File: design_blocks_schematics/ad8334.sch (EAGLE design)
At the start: 68 parts, among them IC1 AD8334ACPZ

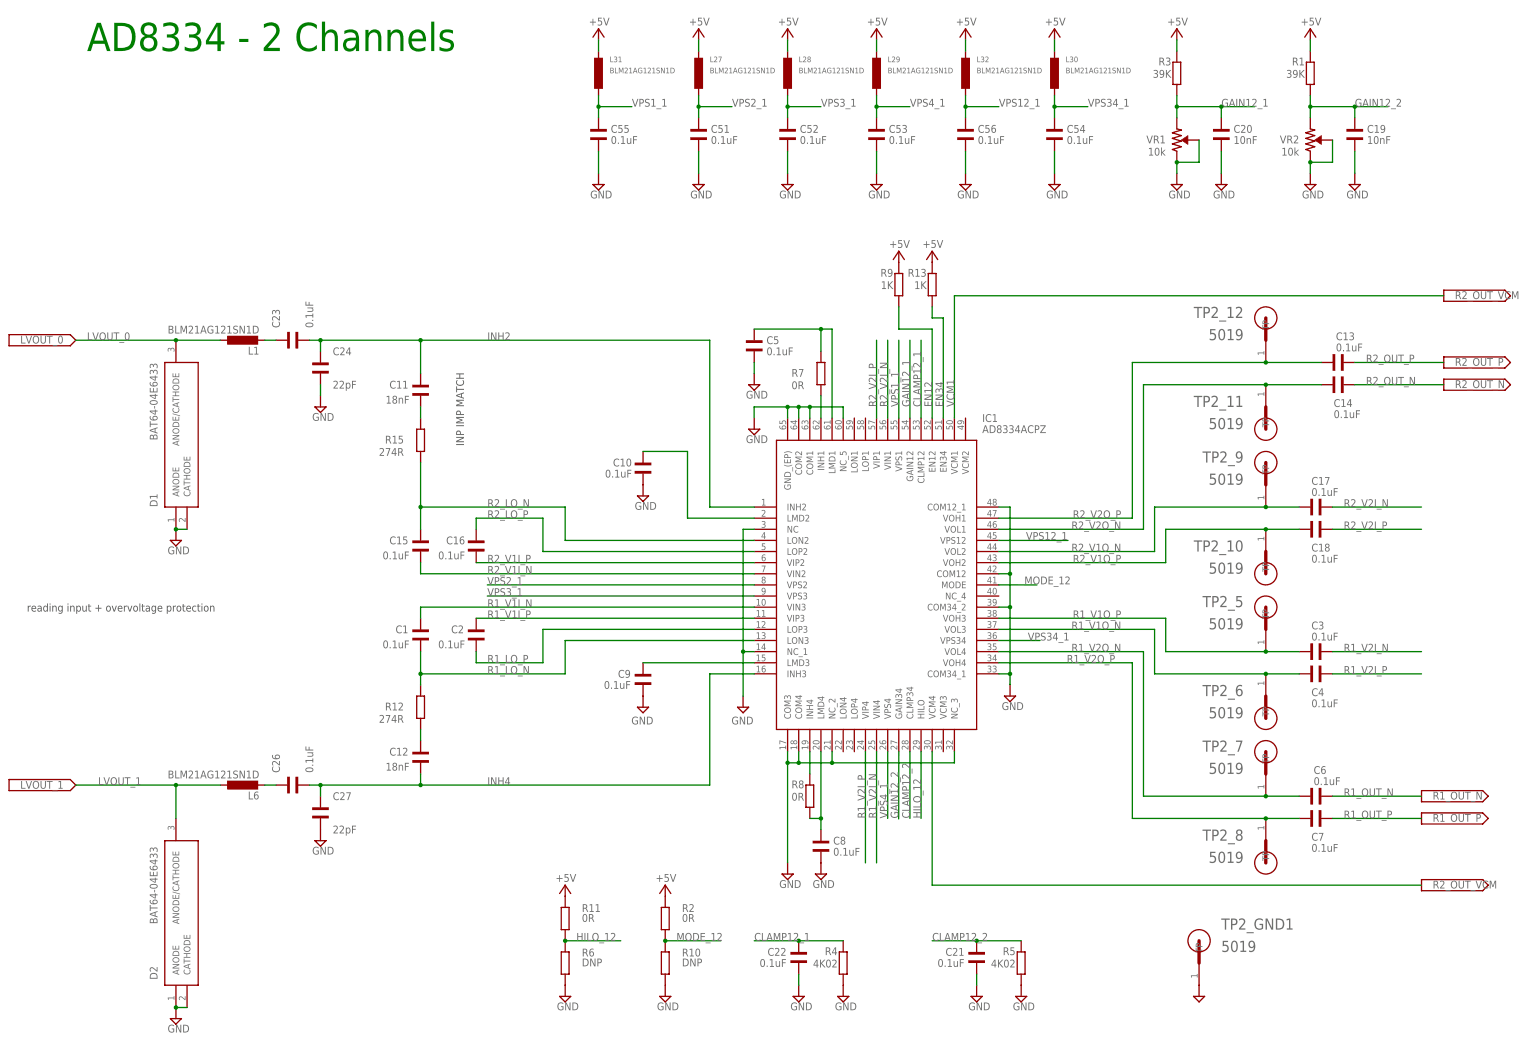
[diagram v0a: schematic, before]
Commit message: updated input/output net names
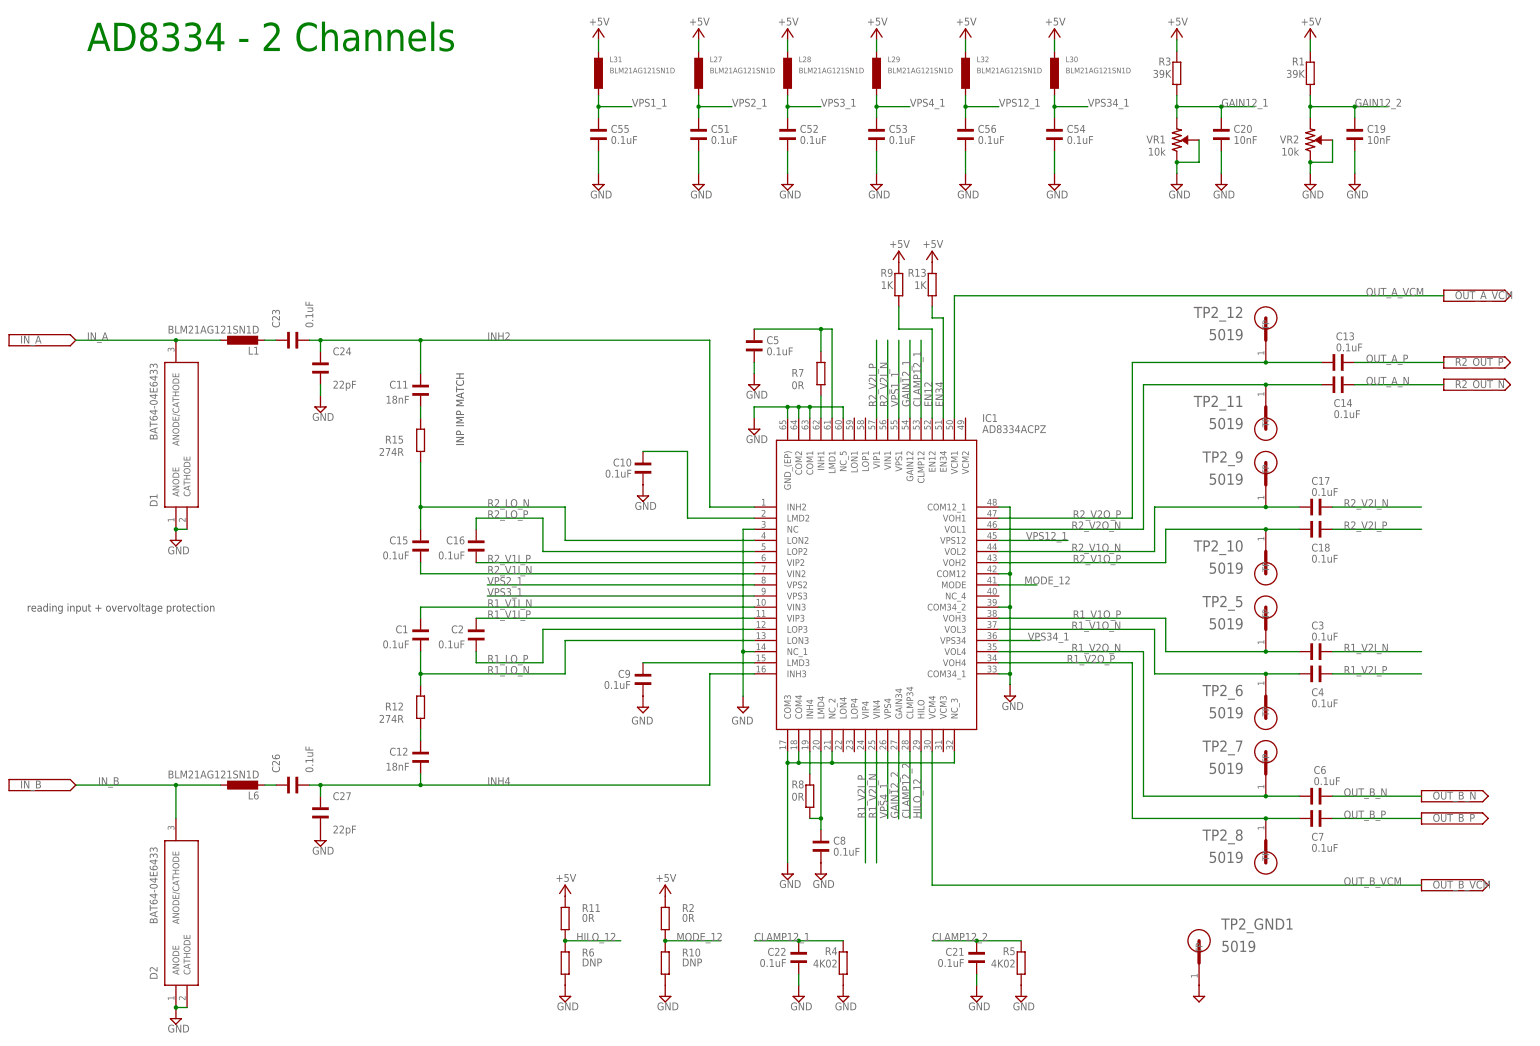
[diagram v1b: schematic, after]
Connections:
- net LVOUT_0 renamed IN_A
- net LVOUT_1 renamed IN_B
- net R1_OUT_N renamed OUT_B_N
- net R1_OUT_P renamed OUT_B_P
- net R2_OUT_N renamed OUT_A_N
- net R2_OUT_P renamed OUT_A_P
- net VCM1 renamed OUT_A_VCM
- net VCM3 renamed OUT_B_VCM
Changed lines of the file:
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@@
 <setting verticaltext="up"/>
 </settings>
-<grid distance="1" unitdist="mm" unit="mm" style="lines" multiple="1" display="no" altdistance="0.5" altunitdist="mm" altunit="mm"/>
+<grid distance="0.1" unitdist="inch" unit="inch" style="lines" multiple="1" display="yes" altdistance="0.01" altunitdist="inch" altunit="inch"/>
 <layers>
 <layer number="1" name="Top" color="4" fill="1" visible="no" active="no"/>
@@
 <part name="FRAME1" library="frames" library_urn="urn:adsk.eagle:library:229" deviceset="A3L-LOC" device=""/>
 <part name="SUPPLY5" library="supply2" library_urn="urn:adsk.eagle:library:372" deviceset="V--&gt;" device="">
-<attribute name="NET" value="LVOUT_0"/>
+<attribute name="NET" value="IN_A"/>
 </part>
 <part name="SUPPLY6" library="supply2" library_urn="urn:adsk.eagle:library:372" deviceset="GND" device=""/>
@@
 <part name="C2" library="Wurth_Elektronik_Passive_Capacitors_rev18b" library_urn="urn:adsk.eagle:library:491551" deviceset="WCAP-CSGP_0402" device="" package3d_urn="urn:adsk.eagle:package:491821/2" technology="_885012205037" value="0.1uF"/>
 <part name="SUPPLY8" library="supply2" library_urn="urn:adsk.eagle:library:372" deviceset="V--&gt;" device="">
-<attribute name="NET" value="LVOUT_0"/>
+<attribute name="NET" value="IN_B"/>
 </part>
 <part name="SUPPLY3" library="supply2" library_urn="urn:adsk.eagle:library:372" deviceset="GND" device=""/>
@@
 </part>
 <part name="SUPPLY17" library="supply2" library_urn="urn:adsk.eagle:library:372" deviceset="V--&gt;" device="">
-<attribute name="NET" value="R1_OUT_N"/>
+<attribute name="NET" value="OUT_B_N"/>
 </part>
 <part name="SUPPLY18" library="supply2" library_urn="urn:adsk.eagle:library:372" deviceset="V--&gt;" device="">
-<attribute name="NET" value="R1_OUT_P"/>
+<attribute name="NET" value="OUT_B_P"/>
 </part>
 <part name="SUPPLY25" library="supply2" library_urn="urn:adsk.eagle:library:372" deviceset="GND" device=""/>
 <part name="SUPPLY9" library="supply2" library_urn="urn:adsk.eagle:library:372" deviceset="V--&gt;" device="">
-<attribute name="NET" value="R2_OUT_VCM"/>
+<attribute name="NET" value="OUT_A_VCM"/>
 </part>
 <part name="SUPPLY10" library="supply2" library_urn="urn:adsk.eagle:library:372" deviceset="V--&gt;" device="">
-<attribute name="NET" value="R2_OUT_VCM"/>
+<attribute name="NET" value="OUT_B_VCM"/>
 </part>
 <part name="P+1" library="supply1" library_urn="urn:adsk.eagle:library:371" deviceset="+5V" device=""/>
@@
 <instance part="SUPPLY8" gate="G$1" x="5.08" y="68.58" smashed="yes">
 <attribute name="VALUE" x="6.35" y="67.818" size="1.778" layer="96" display="off"/>
+<attribute name="NET" x="7.62" y="67.818" size="1.778" layer="96"/>
 </instance>
 <instance part="SUPPLY3" gate="GND" x="43.18" y="124.46" smashed="yes">
@@
 </segment>
 </net>
-<net name="VCM1" class="0">
+<net name="OUT_A_VCM" class="0">
 <segment>
 <pinref part="IC1" gate="G$1" pin="VCM1"/>
 <wire x1="220.98" y1="152.4" x2="220.98" y2="180.34" width="0.1524" layer="91"/>
-<label x="220.98" y="154.94" size="1.778" layer="95" rot="R270" align="top-right"/>
+<label x="314.96" y="180.34" size="1.778" layer="95" rot="R180" align="top-right"/>
 <wire x1="220.98" y1="180.34" x2="332.74" y2="180.34" width="0.1524" layer="91"/>
 </segment>
@@
 </segment>
 </net>
-<net name="LVOUT_1" class="2">
-<segment>
-<label x="25.4" y="68.58" size="1.778" layer="95" rot="R180" align="top-right"/>
-<pinref part="D2" gate="G$1" pin="ANODE/CATHODE"/>
-<pinref part="L6" gate="G$1" pin="1"/>
-<wire x1="53.34" y1="68.58" x2="43.18" y2="68.58" width="0.1524" layer="91"/>
-<wire x1="43.18" y1="68.58" x2="20.32" y2="68.58" width="0.1524" layer="91"/>
-<wire x1="43.18" y1="60.96" x2="43.18" y2="68.58" width="0.1524" layer="91"/>
-<junction x="43.18" y="68.58"/>
-</segment>
-<segment>
-<label x="7.62" y="67.7418" size="1.778" layer="95" rot="R180" align="top-right"/>
-</segment>
-</net>
 <net name="VPS1_1" class="0">
 <segment>
@@
 </segment>
 </net>
-<net name="LVOUT_0" class="0">
+<net name="IN_A" class="0">
 <segment>
 <pinref part="D1" gate="G$1" pin="ANODE/CATHODE"/>
@@
 </segment>
 </net>
-<net name="R1_OUT_N" class="0">
+<net name="OUT_B_N" class="0">
 <segment>
 <pinref part="C6" gate="G$1" pin="2"/>
@@
 </segment>
 </net>
-<net name="R1_OUT_P" class="0">
+<net name="OUT_B_P" class="0">
 <segment>
 <pinref part="C7" gate="G$1" pin="2"/>
@@
 </segment>
 </net>
-<net name="R2_OUT_P" class="0">
+<net name="OUT_A_P" class="0">
 <segment>
 <pinref part="C13" gate="G$1" pin="2"/>
@@
 </segment>
 </net>
-<net name="R2_OUT_N" class="0">
+<net name="OUT_A_N" class="0">
 <segment>
 <pinref part="C14" gate="G$1" pin="2"/>
@@
 </segment>
 </net>
-<net name="VCM3" class="0">
+<net name="OUT_B_VCM" class="0">
 <segment>
 <wire x1="215.9" y1="45.72" x2="327.66" y2="45.72" width="0.1524" layer="91"/>
 <pinref part="IC1" gate="G$1" pin="VCM4"/>
 <wire x1="215.9" y1="76.2" x2="215.9" y2="45.72" width="0.1524" layer="91"/>
+<label x="309.88" y="45.72" size="1.778" layer="95"/>
 </segment>
 </net>
@@
 </segment>
 </net>
+<net name="IN_B" class="2">
+<segment>
+<label x="25.4" y="68.58" size="1.778" layer="95" rot="R180" align="top-right"/>
+<pinref part="D2" gate="G$1" pin="ANODE/CATHODE"/>
+<pinref part="L6" gate="G$1" pin="1"/>
+<wire x1="53.34" y1="68.58" x2="43.18" y2="68.58" width="0.1524" layer="91"/>
+<wire x1="43.18" y1="68.58" x2="20.32" y2="68.58" width="0.1524" layer="91"/>
+<wire x1="43.18" y1="60.96" x2="43.18" y2="68.58" width="0.1524" layer="91"/>
+<junction x="43.18" y="68.58"/>
+</segment>
+</net>

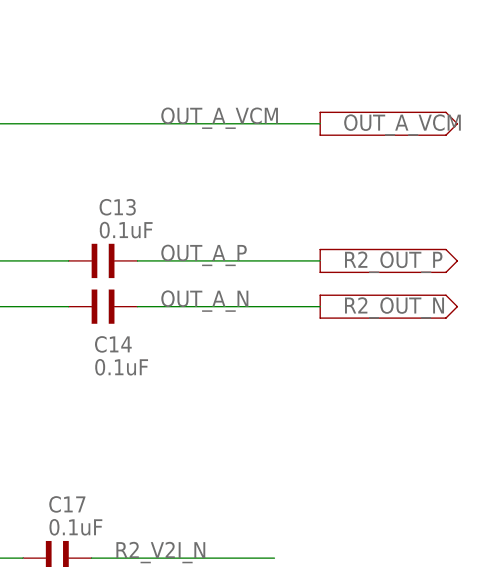
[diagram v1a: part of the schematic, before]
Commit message: updated input/output net names
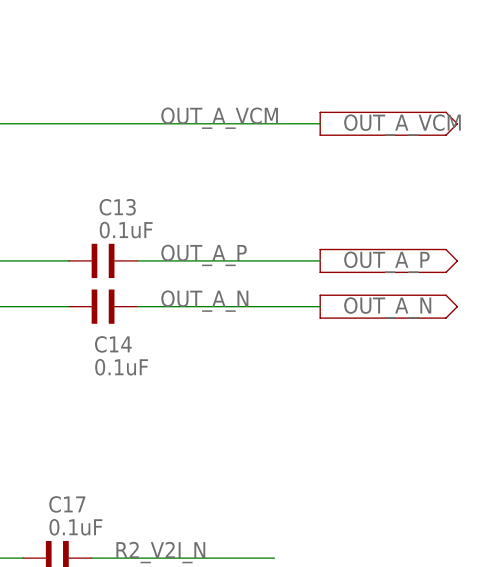
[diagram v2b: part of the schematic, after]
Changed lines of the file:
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@@
 <part name="C7" library="Wurth_Elektronik_Passive_Capacitors_rev18b" library_urn="urn:adsk.eagle:library:491551" deviceset="WCAP-CSGP_0402" device="" package3d_urn="urn:adsk.eagle:package:491821/2" technology="_885012205037" value="0.1uF"/>
 <part name="SUPPLY15" library="supply2" library_urn="urn:adsk.eagle:library:372" deviceset="V--&gt;" device="">
-<attribute name="NET" value="R2_OUT_P"/>
+<attribute name="NET" value="OUT_A_P"/>
 </part>
 <part name="SUPPLY16" library="supply2" library_urn="urn:adsk.eagle:library:372" deviceset="V--&gt;" device="">
-<attribute name="NET" value="R2_OUT_N"/>
+<attribute name="NET" value="OUT_A_N"/>
 </part>
 <part name="SUPPLY17" library="supply2" library_urn="urn:adsk.eagle:library:372" deviceset="V--&gt;" device="">
